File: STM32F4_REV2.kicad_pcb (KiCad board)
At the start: 4 copper layers, 56 x 51 mm, 54 parts, among them J1 Screw_Terminal_01x02, J2 SWD, J3 Conn_01x04, J4 Conn_01x04, J5 USB_B_Micro, Q1 AO3401A, SW1 SW_SPDT, U1 MP2359DJ-LF-Z, U2 STM32F405RGT6, U3 USBLC6-2SC6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

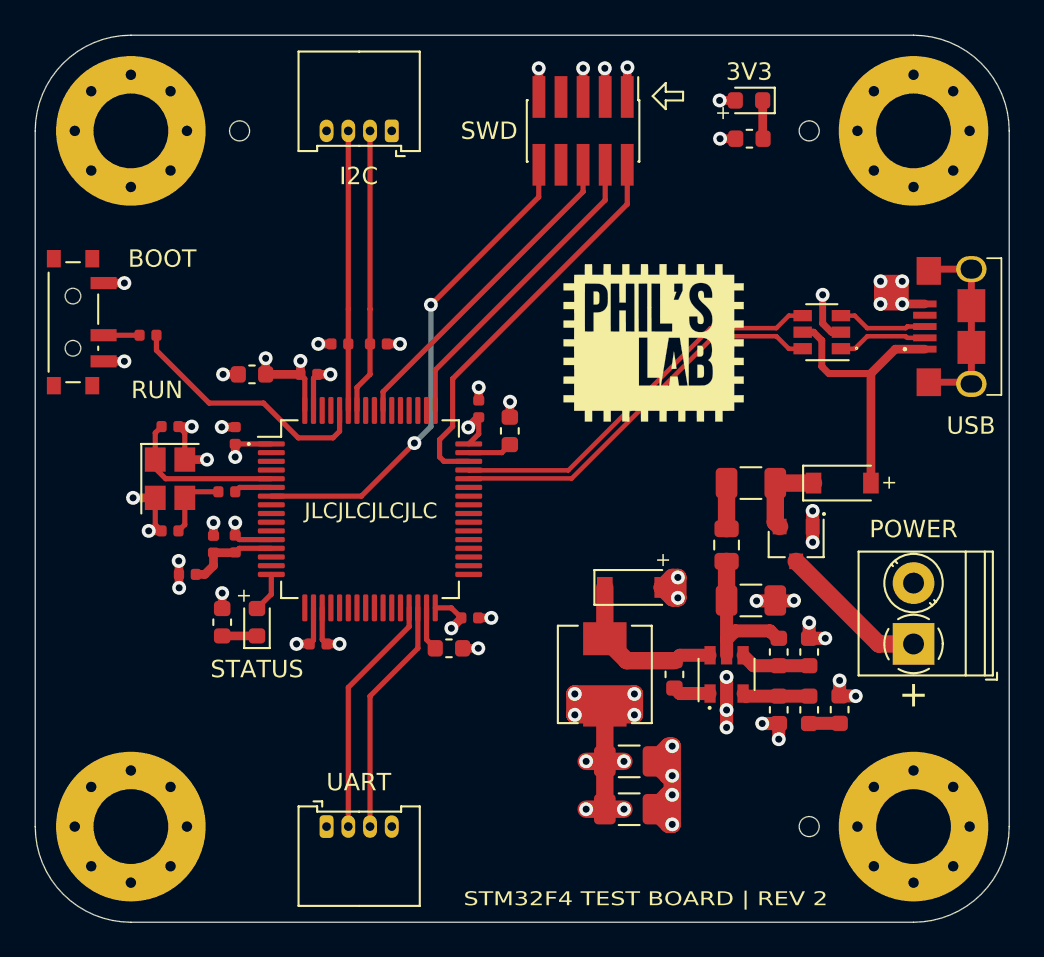
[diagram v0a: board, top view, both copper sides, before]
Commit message: initial commit :STM32F4 Reference PCB
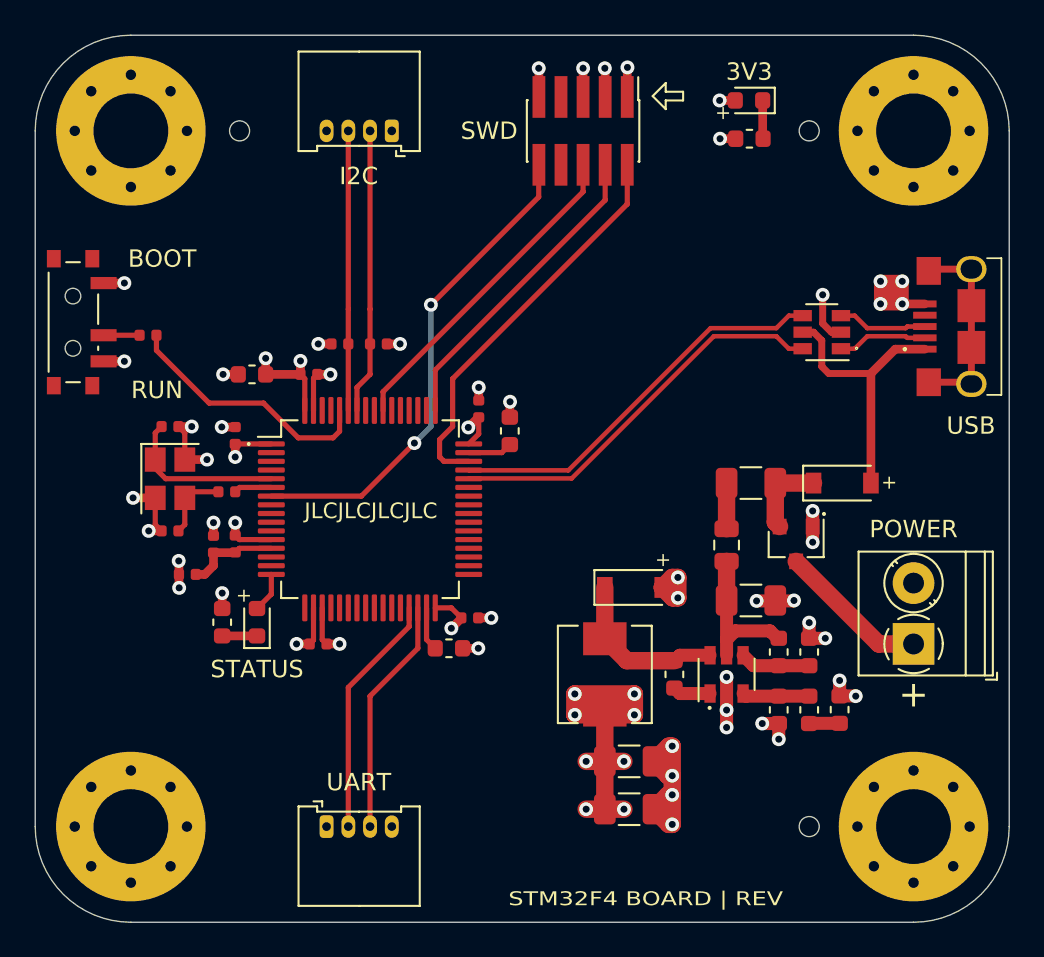
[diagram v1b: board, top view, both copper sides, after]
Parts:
- removed G***: LOGO, SchmillipKiCADLibrary:Silk_PhilsLabIC
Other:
- net class Default removed
- board text added: "STM32F4 BOARD | REV"
- board text removed: "STM32F4 TEST BOARD | REV 2"
